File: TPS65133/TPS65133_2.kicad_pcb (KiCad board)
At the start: 2 copper layers, 19.8 x 50.3 mm, 16 parts, among them U1 TPS65133DPDR

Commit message: New components
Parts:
- +3.3V, +5V, -5V: value (none) -> 02x03_Male
- C1, C5, C6: value GRM21BR71E104KA01 -> (none)
- C2: value GRM21BR71A106KE51 -> (none)
- C3, C4: value GRM21BR71A106KE5 -> (none)
- L1, L2: value 1239AS-H-4R7M=P2 -> (none)
- U1: value TPS65133DPDR -> (none)

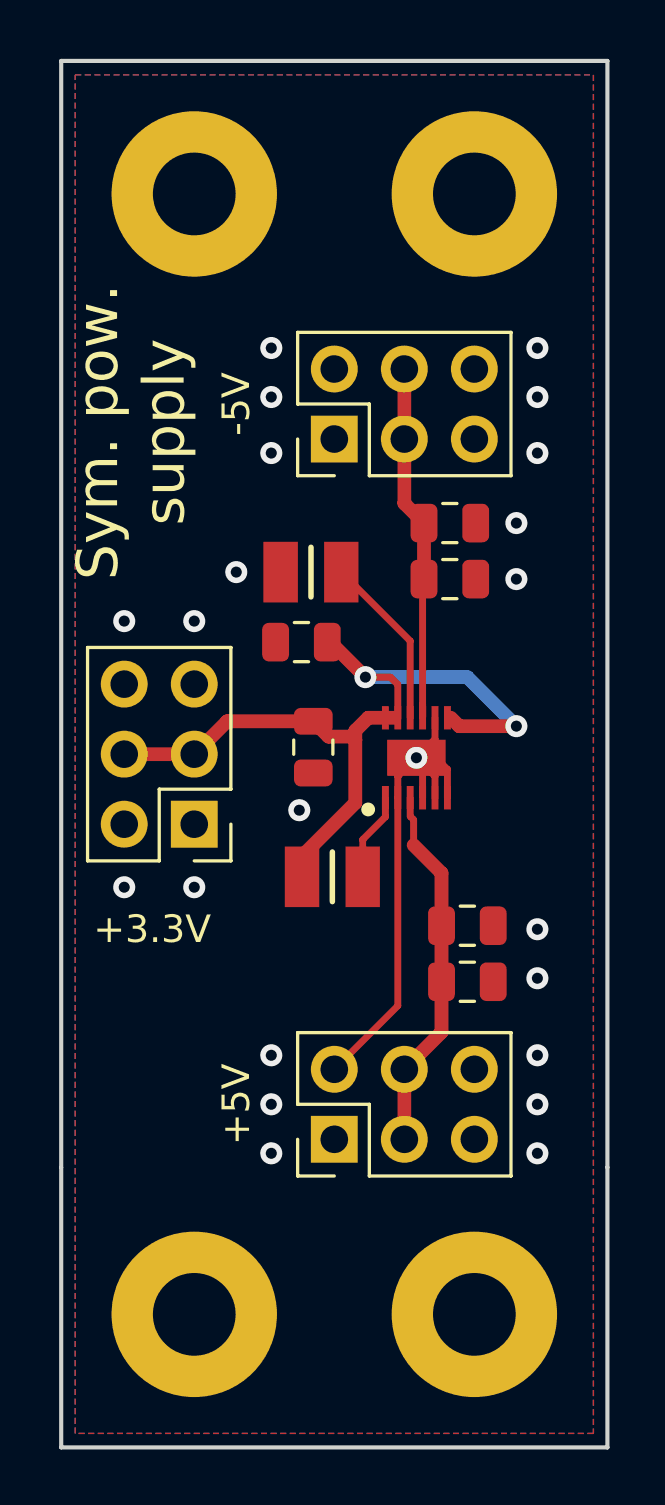
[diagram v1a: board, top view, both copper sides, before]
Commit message: upravy, pred vyrobou, opraven problem s maskou
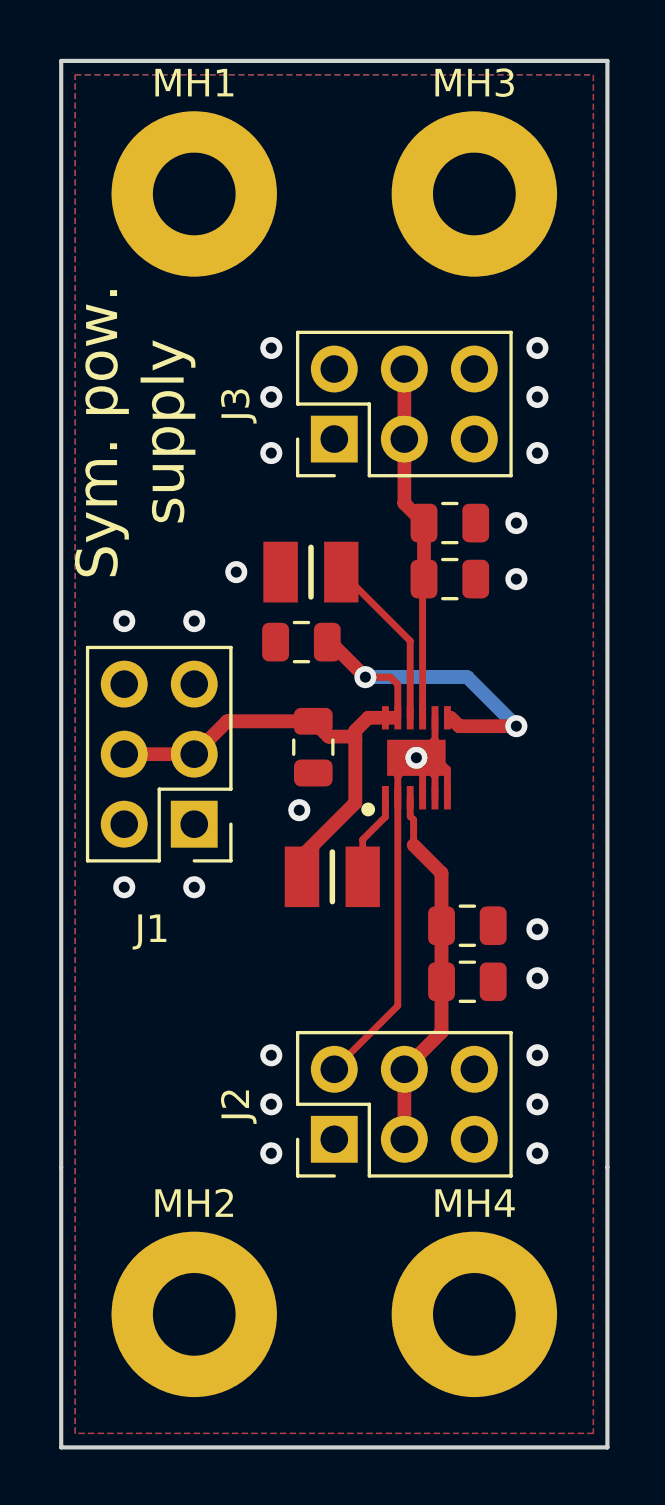
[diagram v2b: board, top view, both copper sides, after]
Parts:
- C1, C5, C6: value (none) -> 0.1uF
- C2, C3, C4: value (none) -> 10uF
- IC1: renamed from U1; value (none) -> TPS65133DPDR; footprint SamacSys_Parts:SON45P300X300X80-13N-D -> Mlab_IO:SON45P300X300X80-13N-D
- J1: renamed from +3.3V; value 02x03_Male -> Conn_02x03_Odd_Even
- J2: renamed from +5V; value 02x03_Male -> Conn_02x03_Odd_Even
- J3: renamed from -5V; value 02x03_Male -> Conn_02x03_Odd_Even
- L1, L2: value (none) -> 1239AS-H-4R7M=P2; footprint SamacSys_Parts:1239AS-H-4R7M=P2 -> Resistor_SMD:1239AS-H-4R7M=P2
- MH1, MH2, MH3, MH4: renamed from ?; value (none) -> MountingHole_Pad
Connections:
- MH1 pad 1: Net-(MH1-Pad1) -> (no net)
- MH2 pad 1: Net-(MH2-Pad1) -> (no net)
- MH3 pad 1: Net-(MH3-Pad1) -> (no net)
- MH4 pad 1: Net-(MH4-Pad1) -> (no net)
